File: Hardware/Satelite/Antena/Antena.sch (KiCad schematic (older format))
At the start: 4 parts, among them J1 Conn_01x01, J2 Conn_01x01

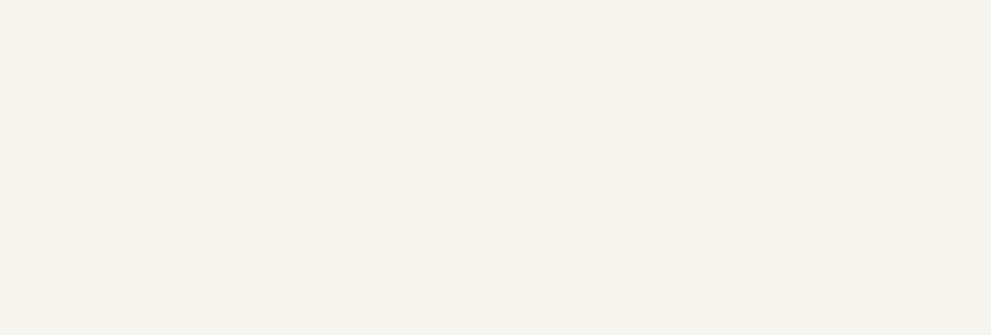
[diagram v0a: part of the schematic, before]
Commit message: Añadida información faltante en rótulos de los esquemas
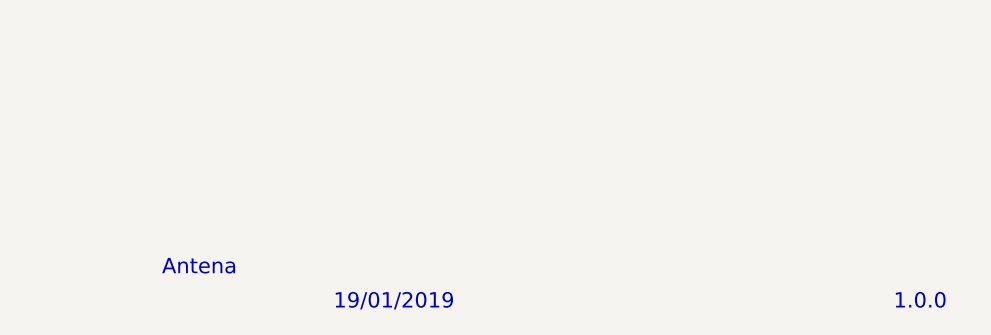
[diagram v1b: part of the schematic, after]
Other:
- note added: "1.0.0"
- note added: "19/01/2019"
- note added: "Antena"
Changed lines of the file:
@@
 EndData
 $EndBitmap
+Text Notes 7400 7500 0    67   ~ 0
+Antena
+Text Notes 10600 7650 0    67   ~ 0
+1.0.0
+Text Notes 8150 7650 0    67   ~ 0
+19/01/2019
 $EndSCHEMATC
